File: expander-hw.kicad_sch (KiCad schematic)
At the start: 67 parts, among them J1 USB_C_Receptacle_USB2.0_16P, J2 Conn_ARM_JTAG_SWD_10, J3 Conn_02x03_Odd_Even, J4 Conn_02x08_Odd_Even, U1 AZ1117-3.3, U10 MCP1501-10xCH, U2 TPS65130RGE, U3 USBLC6-2SC6, U4 STM32H523RETx, U5 SRDA3.3-4BTG, U6 SRDA3.3-4BTG, U7 SRDA3.3-4BTG, U8 DAC8562, U9 OPA2994xD

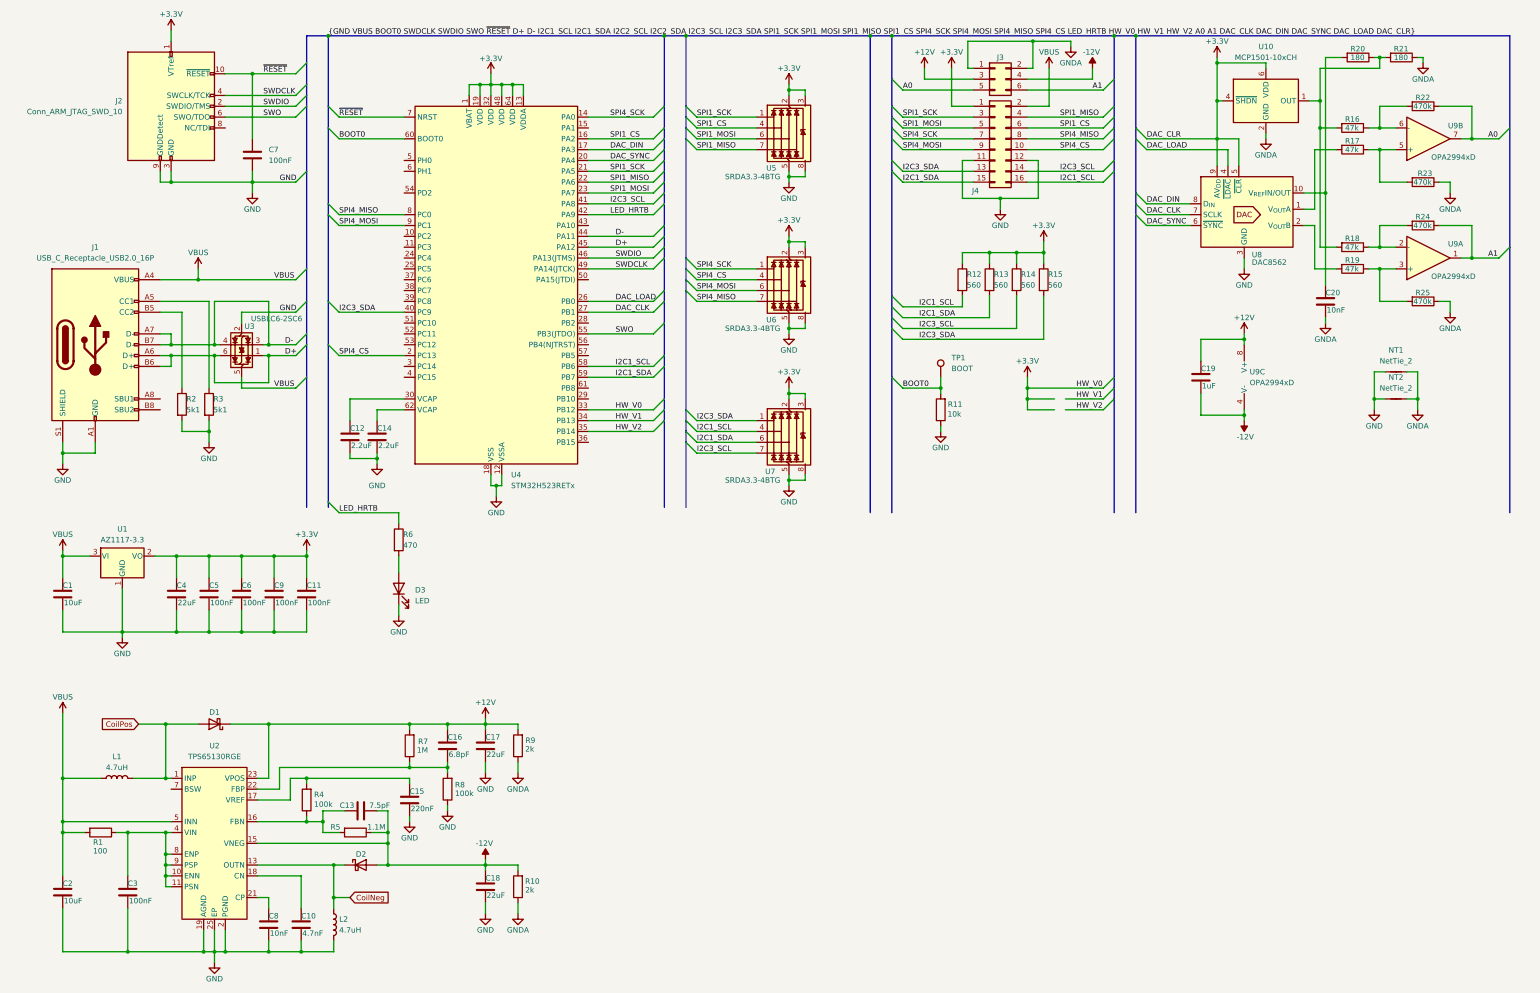
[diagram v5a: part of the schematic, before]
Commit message: Fix converter EMI
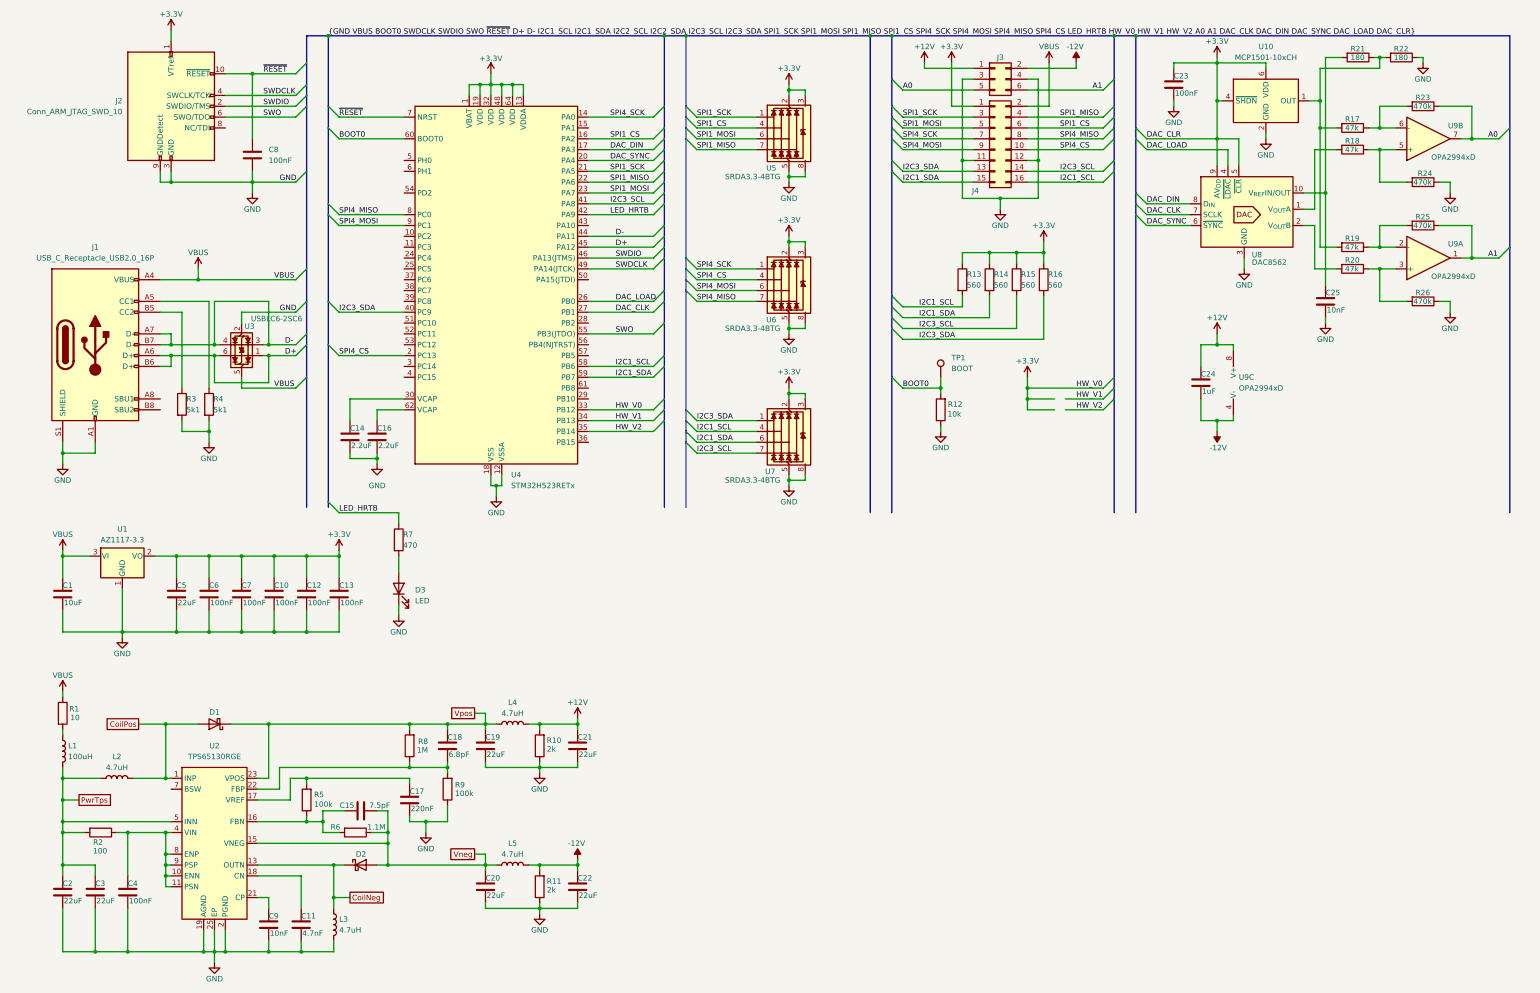
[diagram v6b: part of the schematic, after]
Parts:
- removed NT1, NT2: NetTie_2, NetTie:NetTie-2_SMD_Pad0.5mm, symbol Device:NetTie_2
- added C12, C13: 100nF, Capacitor_SMD:C_0603_1608Metric, symbol Device:C
- added C21, C22, C3: 22uF, Capacitor_SMD:C_0805_2012Metric, symbol Device:C
- added L1: 100uH, Inductor_SMD:L_1210_3225Metric, symbol Device:L
- added L4, L5: 4.7uH, Inductor_SMD:L_1210_3225Metric, symbol Device:L
- added R1: 10, Resistor_SMD:R_0805_2012Metric, symbol Device:R
- C2: value 10uF -> 22uF
- D1, D2: footprint Diode_SMD:D_1206_3216Metric -> Diode_SMD:D_0805_2012Metric
- renumbered C9 to C10, C10 to C11, C12 to C14, C13 to C15, C14 to C16, C15 to C17, C16 to C18, C17 to C19, C18 to C20, C11 to C23, C19 to C24, C20 to C25, C3 to C4, C4 to C5, C5 to C6, C6 to C7, C7 to C8, C8 to C9, L1 to L2, L2 to L3, R9 to R10, R10 to R11, R11 to R12, R12 to R13, R13 to R14, R14 to R15, R15 to R16, R16 to R17, R17 to R18, R18 to R19, R1 to R2, R19 to R20, R20 to R21, R21 to R22, R22 to R23, R23 to R24, R24 to R25, R25 to R26, R2 to R3, R3 to R4, R4 to R5, R5 to R6, R6 to R7, R7 to R8, R8 to R9
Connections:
- net +12V: now also J3.1 (Pin_1), C21.1, L4.2; no longer C18.1, C19.1, D1.1 (K), J3.3 (Pin_3), R8.2, U2.23 (VPOS)
- net +3.3V: now also C12.1, C13.1
- net -12V: now also J3.2 (Pin_2), C22.1, L5.2; no longer C15.2, C20.1, D2.2 (A), J3.4 (Pin_4), R6.1, U2.15 (VNEG)
- net GND: now also C25.2, J3.3 (Pin_3), J3.4 (Pin_4), R10.1, R11.1, R22.1, R24.1, R26.1, U10.2 (GND), U10.3 (GND), U10.5 (GND), C12.2, C13.2, C21.2, C22.2, C3.2
- net VBUS: now also R1.1; no longer C2.1, L2.1, R2.2, U2.5 (INN), U2.6 (INN)
- removed net GNDA: C25.2, J3.1 (Pin_1), J3.2 (Pin_2), R10.1, R11.1, R22.1, R24.1, R26.1, U10.2 (GND), U10.3 (GND), U10.5 (GND)
- new net: L1.1, R1.2
- new net PwrTps: C2.1, C3.1, L1.2, L2.1, R2.2, U2.5 (INN), U2.6 (INN)
- new net Vneg: C15.2, C20.1, D2.2 (A), L5.1, R6.1, U2.15 (VNEG)
- new net Vpos: C18.1, C19.1, D1.1 (K), L4.1, R8.2, U2.23 (VPOS)
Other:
- moved on the sheet: C23, C24, R10, R11, U9C

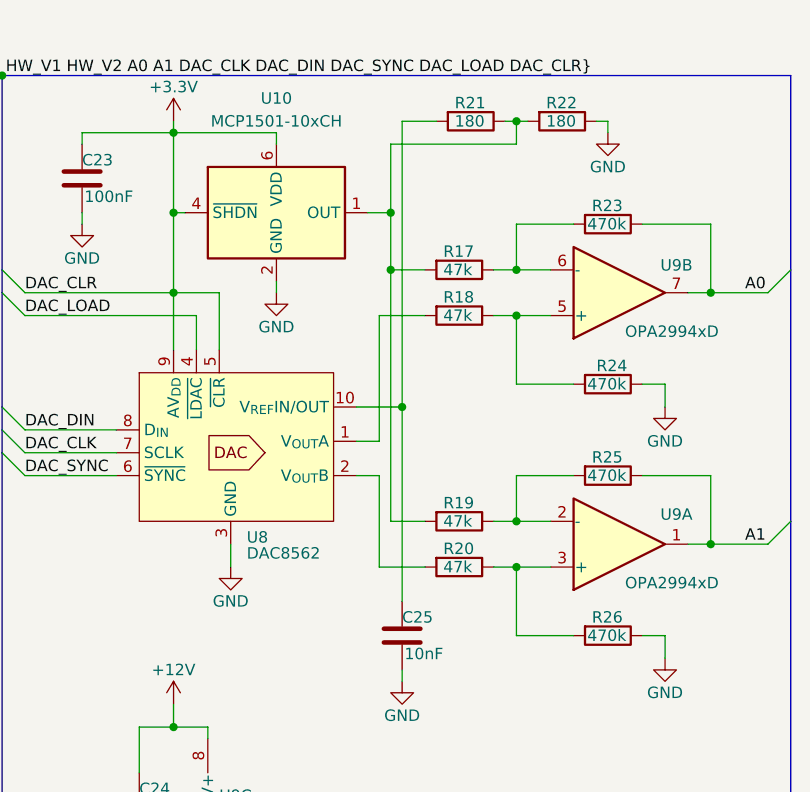
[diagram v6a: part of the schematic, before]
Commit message: Remove Vref divider
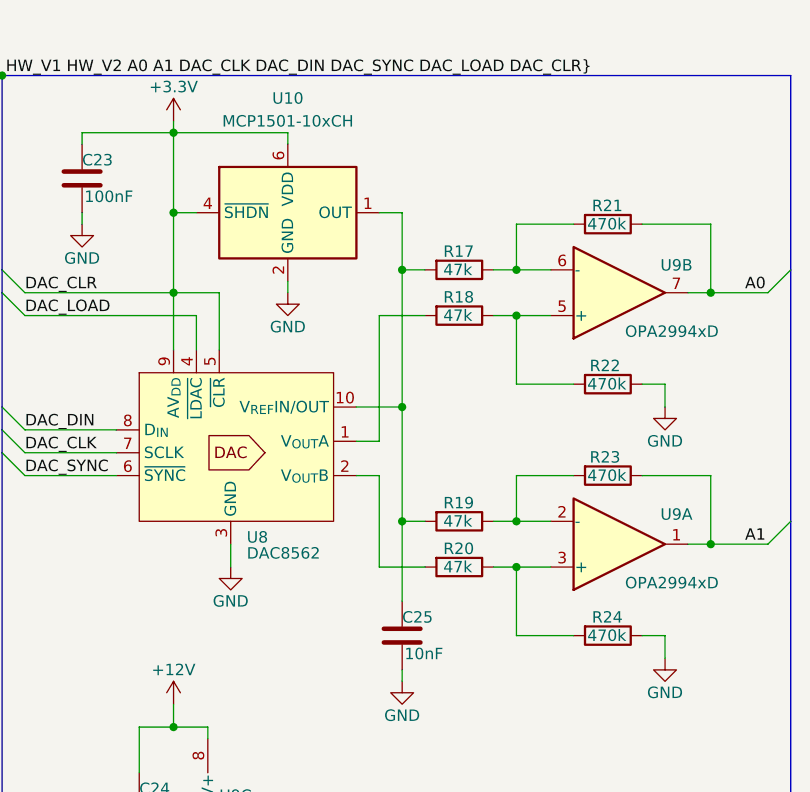
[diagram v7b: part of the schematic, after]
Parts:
- removed R21, R22: 180, Resistor_SMD:R_0603_1608Metric, symbol Device:R
- renumbered R23 to R21, R24 to R22, R25 to R23, R26 to R24
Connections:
- net at R17.2, R19.2, U10.1 (OUT): now also C25.1, U8.10 (V_{REF}IN/OUT)
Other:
- moved on the sheet: U10

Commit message: Add current converter
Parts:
- removed J3: Conn_02x03_Odd_Even, Connector_PinHeader_2.54mm:PinHeader_2x03_P2.54mm_Horizontal, symbol Connector_Generic:Conn_02x03_Odd_Even
- removed J4: Conn_02x08_Odd_Even, Connector_PinHeader_2.54mm:PinHeader_2x08_P2.54mm_Horizontal, symbol Connector_Generic:Conn_02x08_Odd_Even
- removed U3: USBLC6-2SC6, Package_TO_SOT_SMD:SOT-23-6, symbol Power_Protection:USBLC6-2SC6
- removed U5, U6, U7: SRDA3.3-4BTG, Package_SO:SOIC-8_3.9x4.9mm_P1.27mm, symbol expander-hw:TVS-Diode-Array4
- added C26: 1uF, Capacitor_SMD:C_0603_1608Metric, symbol Device:C
- added J3: Conn_02x06_Odd_Even, Connector_PinHeader_2.54mm:PinHeader_2x06_P2.54mm_Horizontal, symbol Connector_Generic:Conn_02x06_Odd_Even
- added J4: Conn_02x04_Odd_Even, Connector_PinHeader_2.54mm:PinHeader_2x04_P2.54mm_Horizontal, symbol Connector_Generic:Conn_02x04_Odd_Even
- added R17, R18: 10k, Resistor_SMD:R_0603_1608Metric, symbol Device:R
- added R23, R24, R25, R26: 1k, Resistor_SMD:R_1206_3216Metric, symbol Device:R
- added R27, R28, R33, R34, R35, R36: 1k, Resistor_SMD:R_0603_1608Metric, symbol Device:R
- added U7: OPA1678, Package_SO:SOIC-8_3.9x4.9mm_P1.27mm, symbol Amplifier_Operational:OPA1678
- renumbered C25 to C24, C24 to C25, R17 to R19, R18 to R20, R19 to R21, R20 to R22, R21 to R29, R22 to R30, R23 to R31, R24 to R32, U4 to U3, U8 to U4, U10 to U5, U9 to U6
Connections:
- net +12V: now also C26.1, J3.1 (Pin_1), U7.8 (V+)
- net +3.3V: now also J3.3 (Pin_3)
- net -12V: now also C26.2, J3.2 (Pin_2), U7.4 (V-)
- net A0: now also J3.7 (Pin_7)
- net A1: now also J3.8 (Pin_8)
- net GND: now also J3.5 (Pin_5), J3.6 (Pin_6), R17.1, R18.1, R27.2, R28.2
- net I2C1_SCL: now also J4.8 (Pin_8)
- net I2C1_SDA: now also J4.7 (Pin_7)
- net I2C3_SCL: now also J4.6 (Pin_6)
- net I2C3_SDA: now also J4.5 (Pin_5)
- net SPI4_CS: now also J4.4 (Pin_4)
- net SPI4_MISO: now also J4.2 (Pin_2)
- net SPI4_MOSI: now also J4.3 (Pin_3)
- net SPI4_SCK: now also J4.1 (Pin_1)
- net VBUS: now also J3.4 (Pin_4)
- new net: R27.1, R33.2, U7.3 (+)
- new net: R25.1, R26.1, R36.2, U7.6 (-)
- new net: R23.1, R24.1, R34.2, U7.2 (-)
- new net: R28.1, R35.2, U7.5 (+)
- new net I0: J3.11 (Pin_11), R33.1, R34.1, U7.1
- new net I1: J3.12 (Pin_12), R35.1, R36.1, U7.7
- new net IIN0: J3.9 (Pin_9), R17.2, R23.2, R24.2
- new net IIN1: J3.10 (Pin_10), R18.2, R25.2, R26.2
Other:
- moved on the sheet: C25, U6C
